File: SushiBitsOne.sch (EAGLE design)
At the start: 58 parts, among them IC1 CH340B, IC2 LM3671-3.3DBV, IC3 TPS562200DBV, J1 ARDUINO_R3, J2 DC-005, Q1 2N7002, Q2 MMBT2222A, U1 STM32F103CBT6-LQFP48, X1 32768Hz, X2 8MHz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

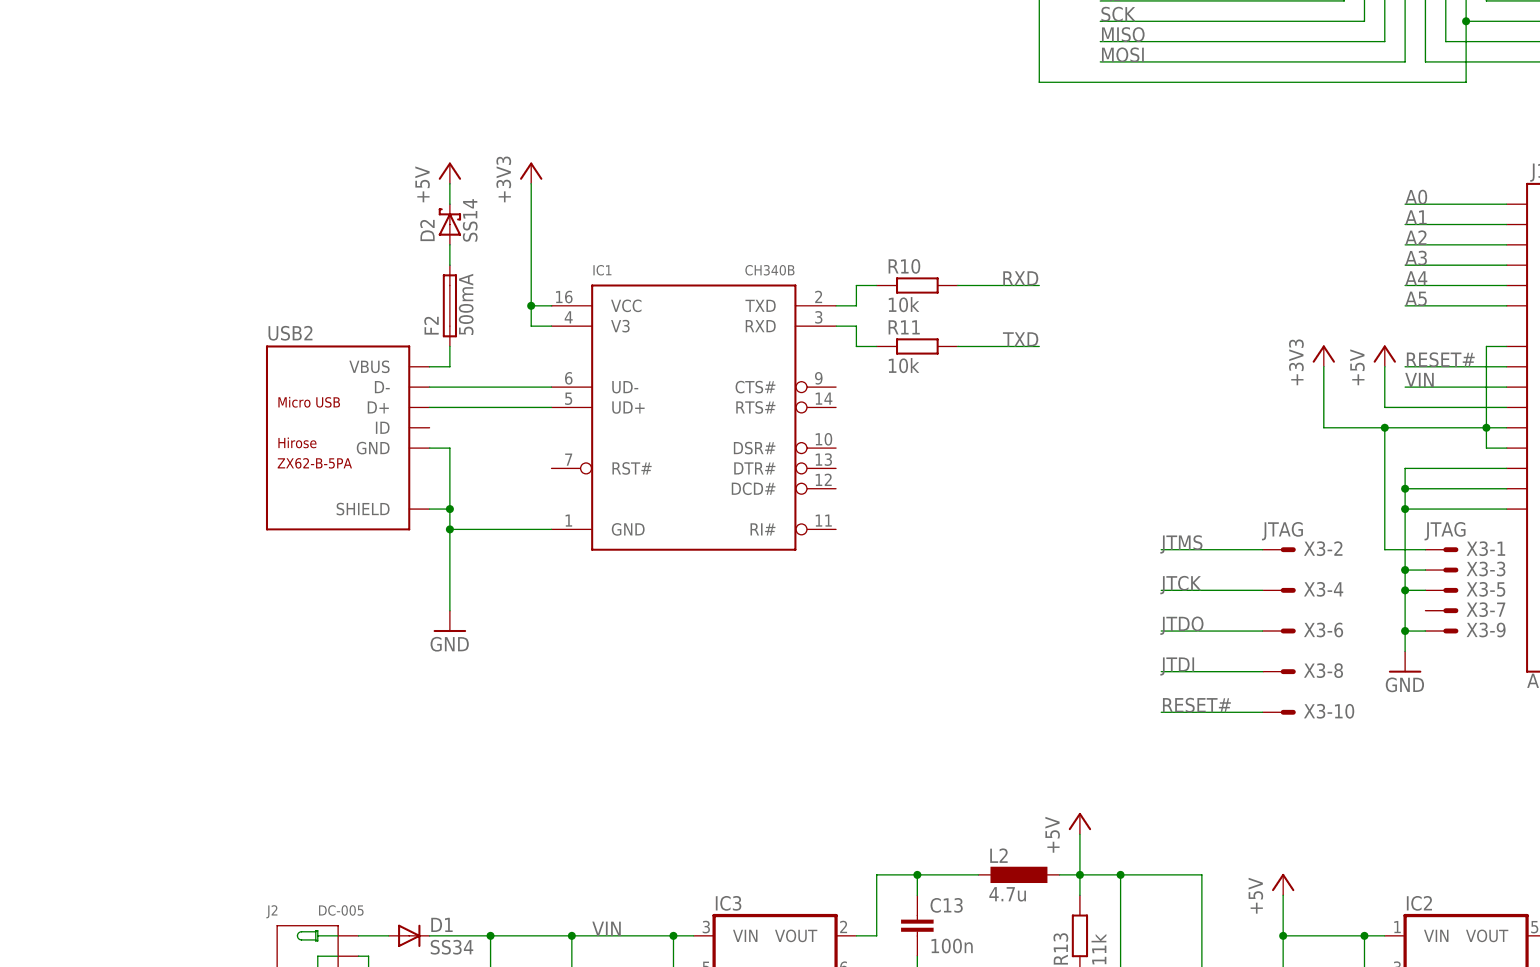
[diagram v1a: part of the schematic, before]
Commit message: Implemented the USB microcontroller with USB-Serial and CMSIS-DAP.
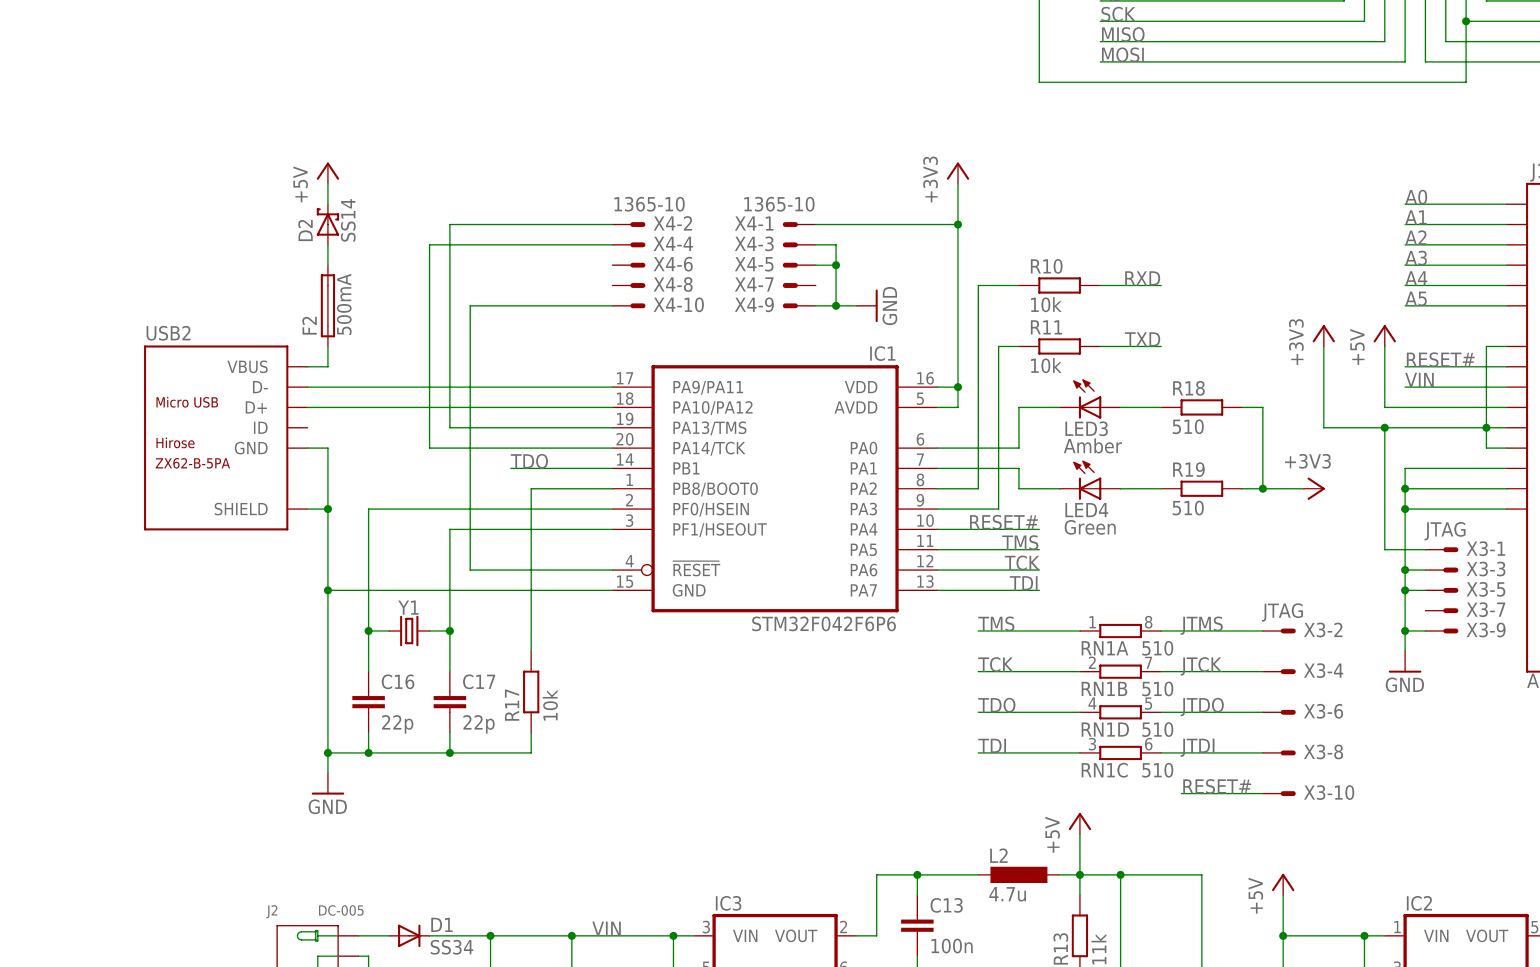
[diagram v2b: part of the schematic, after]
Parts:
- added C16, C17: 22p, rcl:C-EUC0603
- added LED3: Amber, led:LEDCHIPLED_0805
- added LED4: Green, led:LEDCHIPLED_0805
- added R17: 10k, rcl:R-EU_R0603
- added R18, R19: 510, rcl:R-EU_R0603
- added RN1: 510, resistor-dil:4R-NEXB38V
- added X4: 1365-10, con-leotronics:1365-10
- added Y1: (no value), SparkFun-Clocks:CRYSTALSMD-5X3.2-2PAD
- IC1: value CH340B -> STM32F042F6P6; device WCH:CH340B -> HeadphoneBT:STM32F042F6P6
- X2: device SparkFun-Clocks:CRYSTALSMD-5X3.2-4PAD -> SparkFun-Clocks:CRYSTALSMD-5X3.2-2PAD
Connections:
- new net N$21: IC1.PA2, R10.1
- new net N$22: IC1.PA3, R11.1
- new net N$23: IC1.!RESET, X4-10.S
- new net N$24: IC1.PA13/TMS, X4-2.S
- new net N$25: IC1.PA14/TCK, X4-4.S
- new net N$26: IC1.PB8/BOOT0, R17.2
- new net N$27: IC1.PA0, LED3.C
- new net N$28: IC1.PA1, LED4.C
- new net N$29: LED3.A, R18.1
- new net N$30: LED4.A, R19.1
- new net TCK: IC1.PA6, RN1B.1
- new net TDI: IC1.PA7, RN1C.1
- new net TDO: IC1.PB1, RN1D.1
- new net TMS: IC1.PA5, RN1A.1
- net +3V3: now also IC1.AVDD, IC1.VDD, R18.2, R19.2, X4-1.S; no longer IC1.V3, IC1.VCC
- net GND: now also C16.2, C17.2, R17.1, X4-3.S, X4-5.S, X4-9.S
- net JTCK: now also RN1B.2
- net JTDI: now also RN1C.2
- net JTDO: now also RN1D.2
- net JTMS: now also RN1A.2
- net N$3: now also IC1.PA9/PA11; no longer IC1.UD-
- net N$4: now also IC1.PA10/PA12; no longer IC1.UD+
- net N$5: now also C16.1, IC1.PF0/HSEIN, Y1.1; no longer IC1.TXD, R10.1
- net N$6: now also C17.1, IC1.PF1/HSEOUT, Y1.2; no longer IC1.RXD, R11.1
- net RESET#: now also IC1.PA4
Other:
- moved on the sheet: D2, F2, R10, R11, USB2, X3-10, X3-2, X3-4, X3-6, X3-8

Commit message: Releasing M193v4
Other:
- note added: "SushiBits M193v4"
- note removed: "SushiBits M193v3"
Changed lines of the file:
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@@
 <text x="162.56" y="22.86" size="2.54" layer="94" align="top-left">Arduino-compatible STM32
 Development Kit</text>
-<text x="217.17" y="22.86" size="2.54" layer="94" align="top-left">SushiBits M193v3</text>
+<text x="217.17" y="22.86" size="2.54" layer="94" align="top-left">SushiBits M193v4</text>
 <text x="5.08" y="5.08" size="2.54" layer="94">Copyright (c) 2016-2017 Max Chan
 Open Source Hardware. Released under 3-caluse BSD license</text>
